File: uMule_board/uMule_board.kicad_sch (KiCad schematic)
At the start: 1 part, among them J1 12V IN

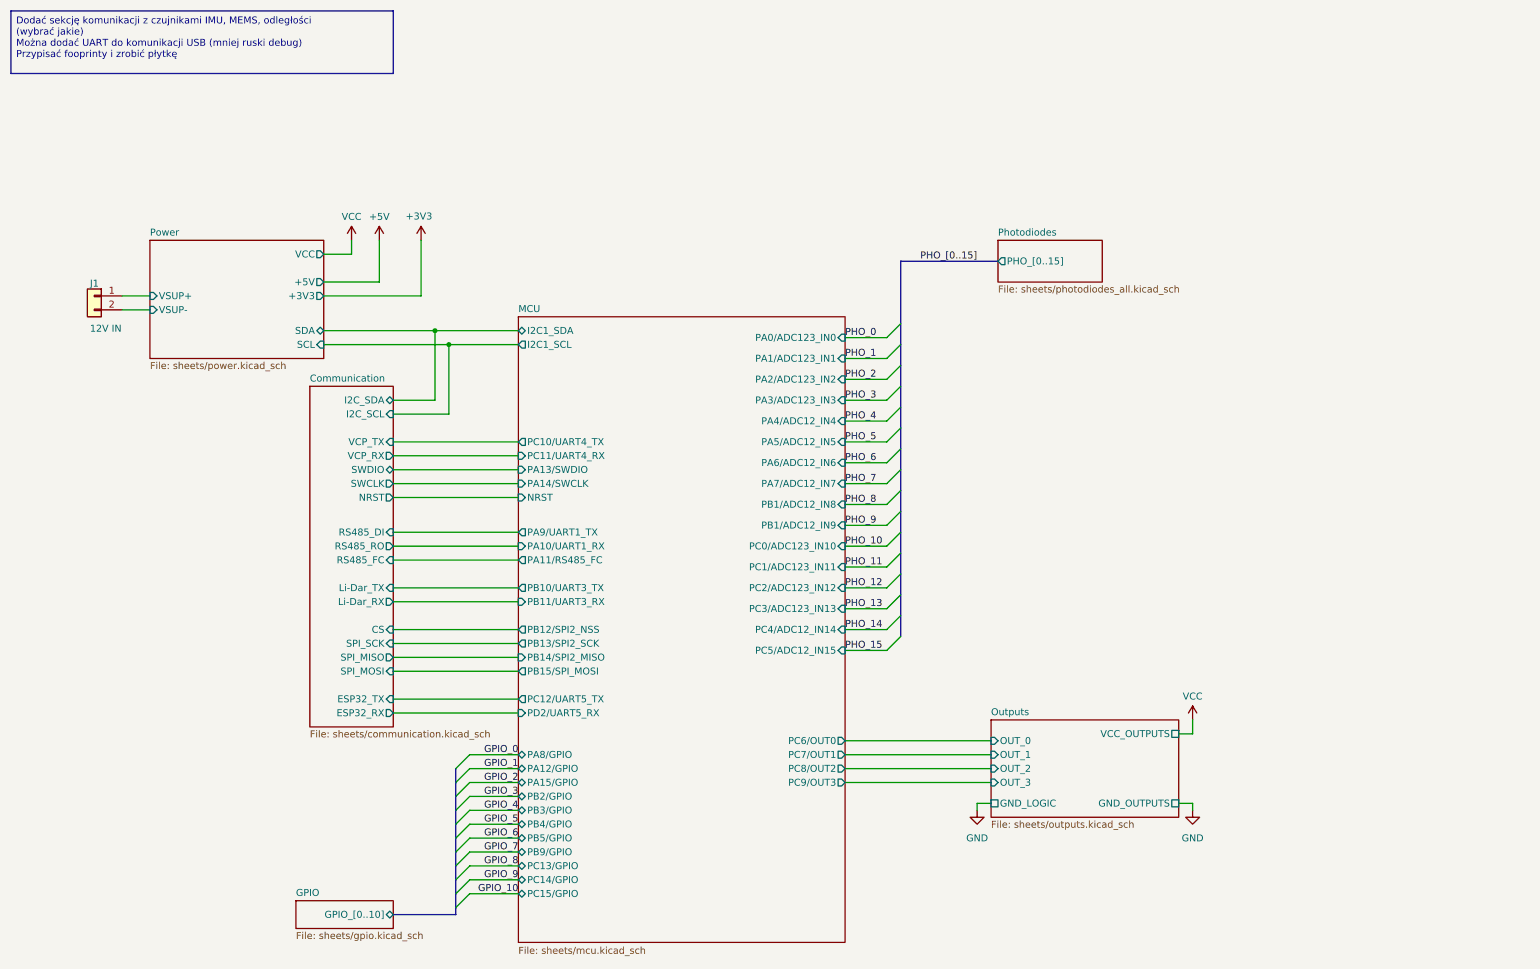
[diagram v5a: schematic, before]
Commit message: Started working on PCB. Ditched high power outputs. Focusing on photodiodes. One commit closer to order
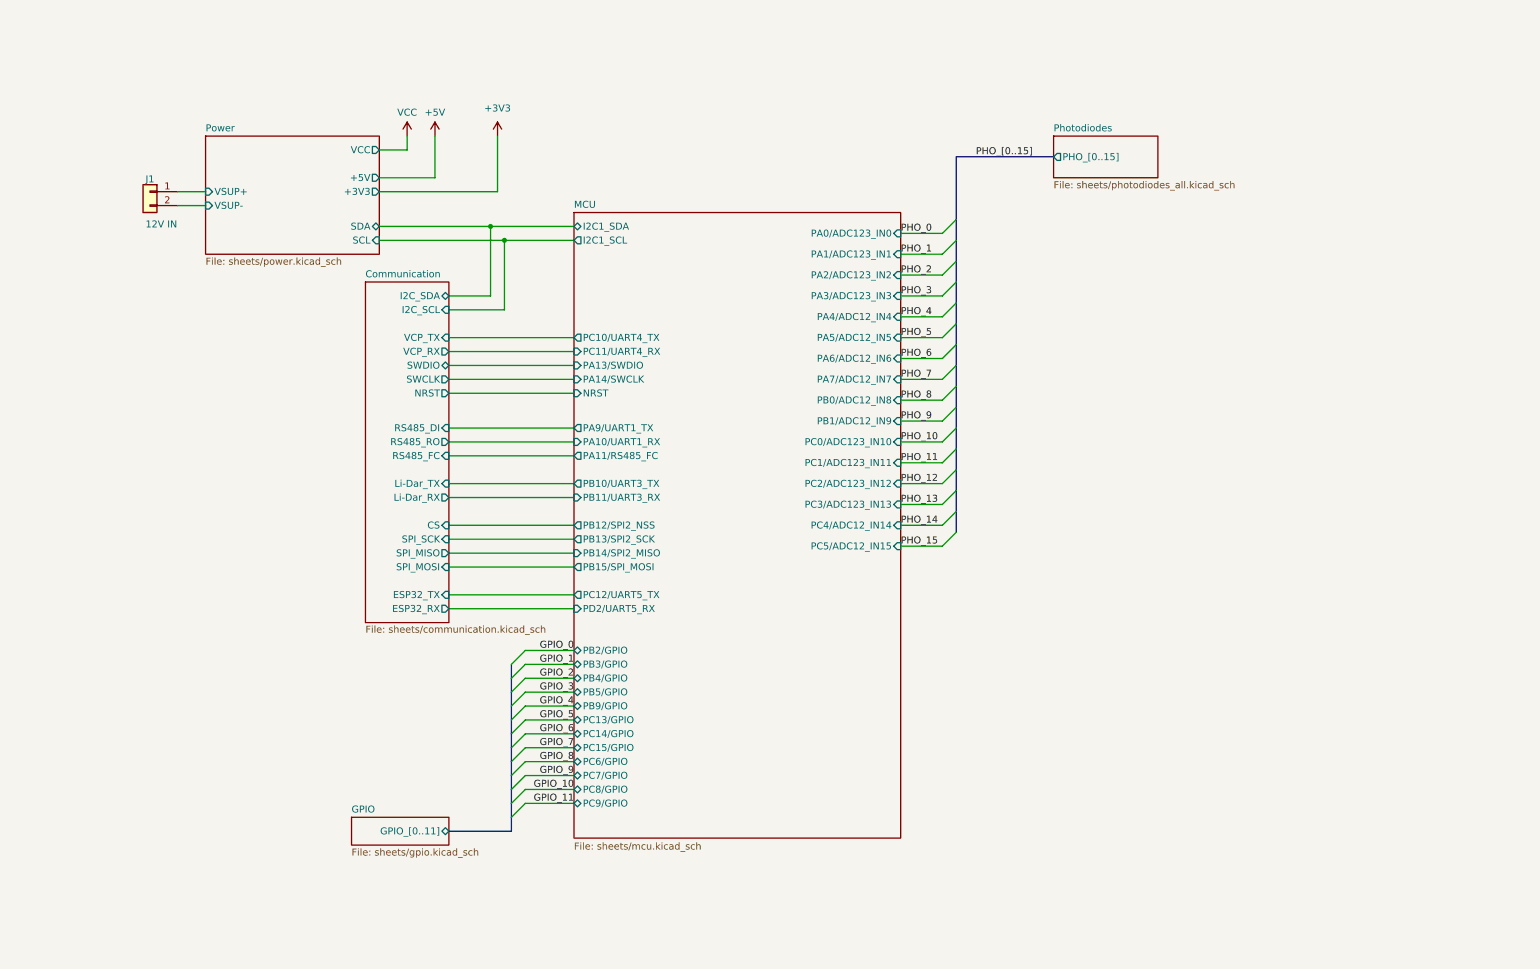
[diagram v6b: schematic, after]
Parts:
- J1: footprint Connector_Phoenix_MC:PhoenixContact_MC_1,5_2-G-3.5_1x02_P3.50mm_Horizontal -> Connector_Phoenix_MC:PhoenixContact_MCV_1,5_2-G-3.5_1x02_P3.50mm_Vertical
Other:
- removed sheet Outputs
- sheet GPIO ports: added GPIO_[0..11]; removed GPIO_[0..10]
- sheet MCU ports: added PB0/ADC12_IN8, PC6/GPIO, PC7/GPIO, PC8/GPIO, PC9/GPIO; removed PA12/GPIO, PA15/GPIO, PA8/GPIO, PB1/ADC12_IN8, PC6/OUT0, PC7/OUT1, PC8/OUT2, PC9/OUT3
- title: (none) -> uMule_board
- moved on the sheet: J1

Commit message: removed half phototransistors, etc.
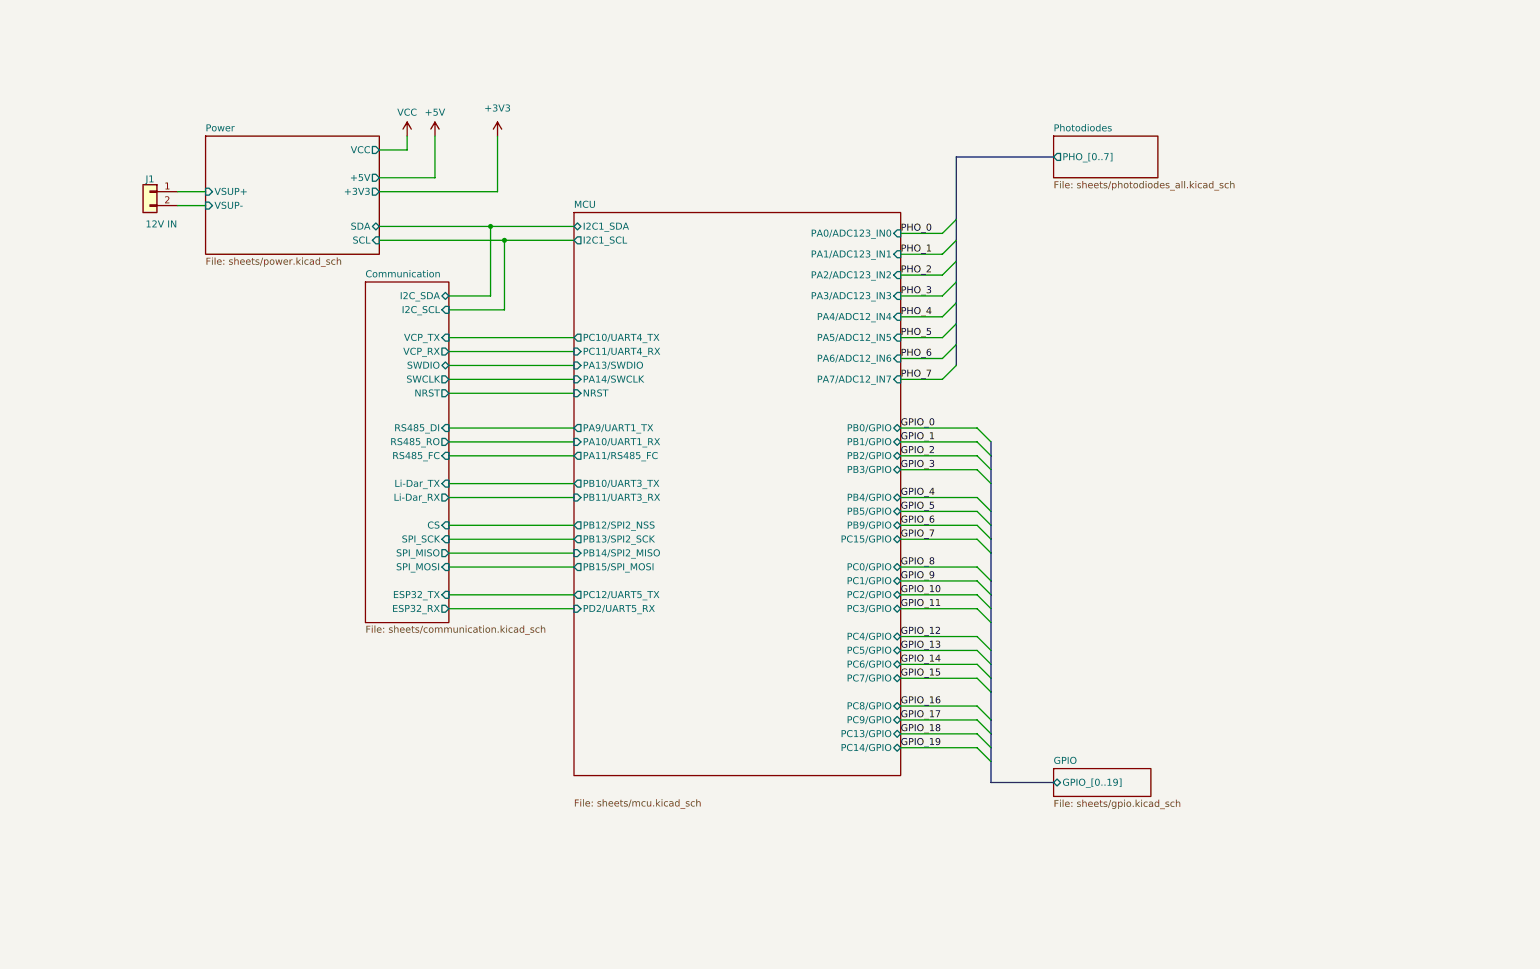
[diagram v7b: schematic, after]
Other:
- sheet GPIO ports: added GPIO_[0..19]; removed GPIO_[0..11]
- sheet MCU ports: added PB0/GPIO, PB1/GPIO, PC0/GPIO, PC1/GPIO, PC2/GPIO, PC3/GPIO, PC4/GPIO, PC5/GPIO; removed PB0/ADC12_IN8, PB1/ADC12_IN9, PC0/ADC123_IN10, PC1/ADC123_IN11, PC2/ADC123_IN12, PC3/ADC123_IN13, PC4/ADC12_IN14, PC5/ADC12_IN15
- sheet Photodiodes ports: added PHO_[0..7]; removed PHO_[0..15]

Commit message: sch ready, only missing the pcb
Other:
- sheet GPIO ports: added GPIO_[1..19]; removed GPIO_[0..19]
- sheet MCU ports: added PB0/ADC12_IN_REF; removed PB0/GPIO
- sheet Photodiodes ports: added V_REF; removed none
- sheet Power ports: added -5V; removed none
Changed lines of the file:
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@@
-	)
-	(bus_entry
-		(at 191.77 91.44)
-		(size -2.54 -2.54)
-		(stroke
-			(width 0)
-			(type default)
-		)
 	)
 	(bus_entry
@@
 	(bus
 		(pts
-			(xy 191.77 91.44) (xy 191.77 93.98)
-		)
-		(stroke
-			(width 0)
-			(type default)
-		)
-	)
-	(bus
-		(pts
 			(xy 191.77 147.32) (xy 191.77 149.86)
 		)
@@
 	(wire
 		(pts
+			(xy 189.23 83.82) (xy 175.26 83.82)
+		)
+		(stroke
+			(width 0)
+			(type default)
+		)
+	)
+	(wire
+		(pts
 			(xy 175.26 80.01) (xy 182.88 80.01)
 		)
@@
 		)
 	)
+	(wire
+		(pts
+			(xy 109.22 35.56) (xy 109.22 48.26)
+		)
+		(stroke
+			(width 0)
+			(type default)
+		)
+	)
 	(bus
 		(pts
@@
 	(wire
 		(pts
+			(xy 189.23 43.18) (xy 189.23 83.82)
+		)
+		(stroke
+			(width 0)
+			(type default)
+		)
+	)
+	(wire
+		(pts
 			(xy 175.26 127) (xy 189.23 127)
 		)
@@
 	(wire
 		(pts
-			(xy 175.26 88.9) (xy 189.23 88.9)
-		)
-		(stroke
-			(width 0)
-			(type default)
-		)
-	)
-	(wire
-		(pts
 			(xy 92.71 91.44) (xy 115.57 91.44)
 		)
@@
 	(wire
 		(pts
+			(xy 203.2 43.18) (xy 189.23 43.18)
+		)
+		(stroke
+			(width 0)
+			(type default)
+		)
+	)
+	(wire
+		(pts
 			(xy 175.26 144.78) (xy 189.23 144.78)
 		)
@@
 		(pts
 			(xy 92.71 111.76) (xy 115.57 111.76)
+		)
+		(stroke
+			(width 0)
+			(type default)
+		)
+	)
+	(wire
+		(pts
+			(xy 109.22 48.26) (xy 80.01 48.26)
 		)
 		(stroke
@@
 		)
 	)
-	(label "GPIO_0"
-		(at 175.26 88.9 0)
-		(effects
-			(font
-				(size 1.27 1.27)
-			)
-			(justify left bottom)
-		)
-	)
 	(label "GPIO_3"
 		(at 175.26 96.52 0)
@@
 			)
 			(justify left bottom)
+		)
+	)
+	(symbol
+		(lib_id "power:-5V")
+		(at 109.22 35.56 0)
+		(unit 1)
+		(exclude_from_sim no)
+		(in_bom yes)
+		(on_board yes)
+		(dnp no)
+		(fields_autoplaced yes)
+		(property "Reference" "#PWR04"
+			(at 109.22 39.37 0)
+			(effects
+				(font
+					(size 1.27 1.27)
+				)
+				(hide yes)
+			)
+		)
+		(property "Value" "-5V"
+			(at 109.22 30.48 0)
+			(effects
+				(font
+					(size 1.27 1.27)
+				)
+			)
+		)
+		(property "Footprint" ""
+			(at 109.22 35.56 0)
+			(effects
+				(font
+					(size 1.27 1.27)
+				)
+				(hide yes)
+			)
+		)
+		(property "Datasheet" ""
+			(at 109.22 35.56 0)
+			(effects
+				(font
+					(size 1.27 1.27)
+				)
+				(hide yes)
+			)
+		)
+		(property "Description" "Power symbol creates a global label with name \"-5V\""
+			(at 109.22 35.56 0)
+			(effects
+				(font
+					(size 1.27 1.27)
+				)
+				(hide yes)
+			)
+		)
+		(pin "1"
+		)
+		(instances
+			(project ""
+				(path "/3d853824-a92e-40a5-ad1a-5052c8a0bd68"
+					(reference "#PWR04")
+					(unit 1)
+				)
+			)
 		)
 	)
@@
 	(sheet
 		(at 203.2 35.56)
-		(size 19.05 7.62)
+		(size 19.05 11.43)
 		(exclude_from_sim no)
 		(in_bom yes)
@@
 		)
 		(property "Sheetfile" "sheets/photodiodes_all.kicad_sch"
-			(at 203.2 43.7646 0)
+			(at 203.2 47.5746 0)
 			(effects
 				(font
@@
 		(pin "PHO_[0..7]" output
 			(at 203.2 39.37 180)
+			(effects
+				(font
+					(size 1.27 1.27)
+				)
+				(justify left)
+			)
+		)
+		(pin "V_REF" output
+			(at 203.2 43.18 180)
 			(effects
 				(font
@@
 			)
 		)
-		(pin "GPIO_[0..19]" bidirectional
+		(pin "GPIO_[1..19]" bidirectional
 			(at 203.2 153.67 180)
 			(effects
@@
 			)
 		)
+		(pin "-5V" output
+			(at 80.01 48.26 0)
+			(effects
+				(font
+					(size 1.27 1.27)
+				)
+				(justify right)
+			)
+		)
 		(instances
 			(project "uMule_board"
@@
 			)
 		)
-		(pin "PB0{slash}GPIO" bidirectional
-			(at 175.26 88.9 0)
-			(effects
-				(font
-					(size 1.27 1.27)
-				)
-				(justify right)
-			)
-		)
 		(pin "PB1{slash}GPIO" bidirectional
 			(at 175.26 91.44 0)
@@
 			(effects
 				(font
+					(size 1.27 1.27)
+				)
+				(justify right)
+			)
+		)
+		(pin "PB0{slash}ADC12_IN_REF" input
+			(at 175.26 83.82 0)
+			(effects
+				(font
